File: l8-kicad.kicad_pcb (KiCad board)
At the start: 4 copper layers, 55.5 x 89.5 mm, 139 parts, among them J1 USB_B_Mini, J2 LCD 3.2" 240x320 Conn_01x14_P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, J3 Screw_Terminal_01x06, J4 Conn_ST_STDC14, J7 TC2030 - TAG Connect, Q1 SI2301CDS-T1-GE3, Q4 SI2301CDS-T1-GE3, Q5 SI2301CDS-T1-GE3, SW1 SW_Push, SW2 SW_Push, U1 B0505S-1WR2, U2 ISO1042-Q1, U22 TLV76733DRVx, U3 STM32F427V_G-I_Tx, U4 ST_SENSOR_2, U5 IIS3DHHCTR, X1 8MHz 20pF

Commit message: pre quilter - actually saved
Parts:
- added TP39: PD10, TestPoint:TestPoint_Pad_D1.0mm, F.Cu at (217.2, 168.3)
- added TP40: PD11, TestPoint:TestPoint_Pad_D1.0mm, F.Cu at (217.2, 171.3)
- TP27: value PD15 -> PD6
- TP28: value PD14 -> PD7
- TP29: value PD13 -> PD8
- TP30: value PD12 -> PD9
- moved TP10 169.7 mm to (217.2, 151.6)
- moved TP11 169.7 mm to (217.2, 154.6)
- moved TP12 169.7 mm to (217.2, 157.7)
- moved TP13 169.7 mm to (217.2, 160.7)
- moved TP14 169.7 mm to (217.2, 163.8)
- moved TP15 169.7 mm to (220.2, 145.4)
- moved TP16 169.7 mm to (220.2, 148.5)
- moved TP17 169.7 mm to (220.2, 151.6)
- moved TP18 169.7 mm to (220.2, 154.6)
- moved TP19 169.7 mm to (220.2, 157.7)
- moved TP20 169.7 mm to (220.2, 160.7)
- moved TP21 169.7 mm to (220.2, 163.8)
- moved TP22 169.7 mm to (223.2, 145.4)
- moved TP23 169.7 mm to (223.2, 148.5)
- moved TP24 169.7 mm to (223.2, 151.6)
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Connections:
- TP27 pad 1: /MCU/PD15 -> /MCU/PD6
- TP28 pad 1: /MCU/PD14 -> /MCU/PD7
- TP29 pad 1: /MCU/PD13 -> /MCU/PD8
- TP30 pad 1: /MCU/PD12 -> /MCU/PD9

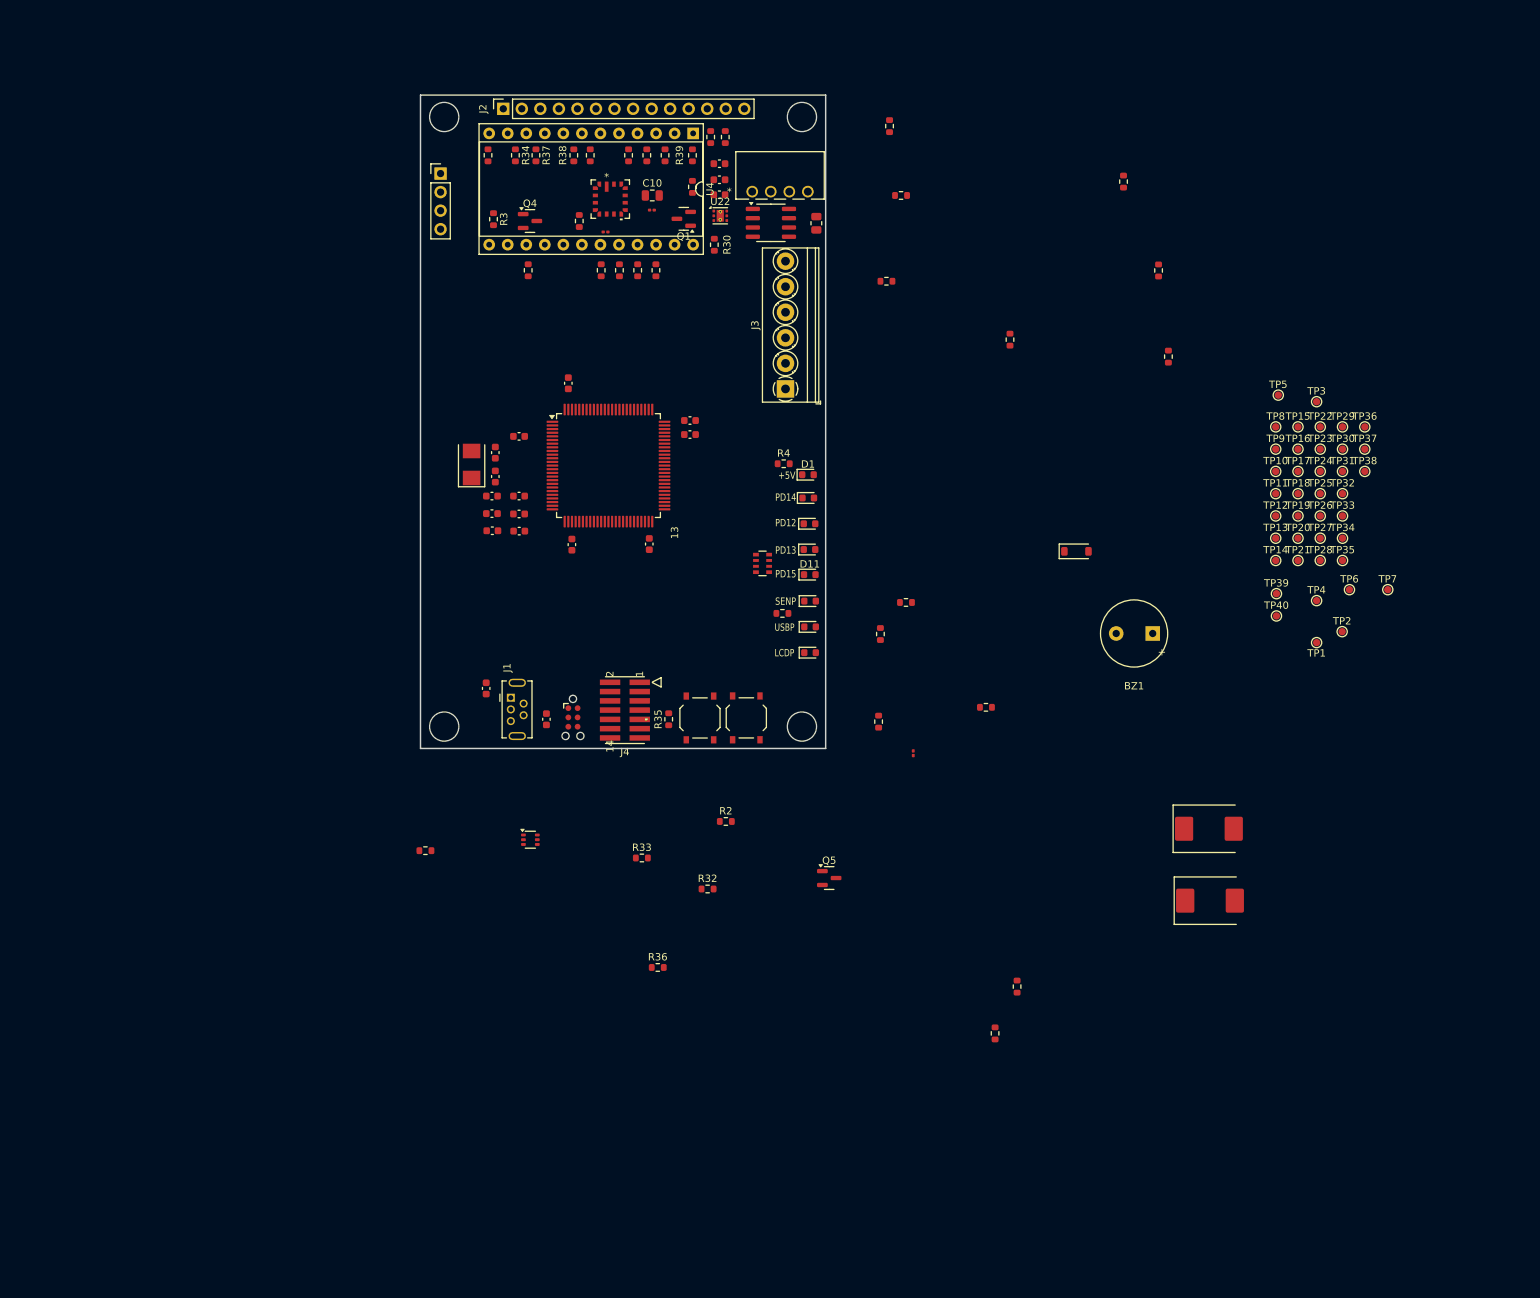
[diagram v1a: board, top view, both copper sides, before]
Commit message: remove tp and rotate cpu
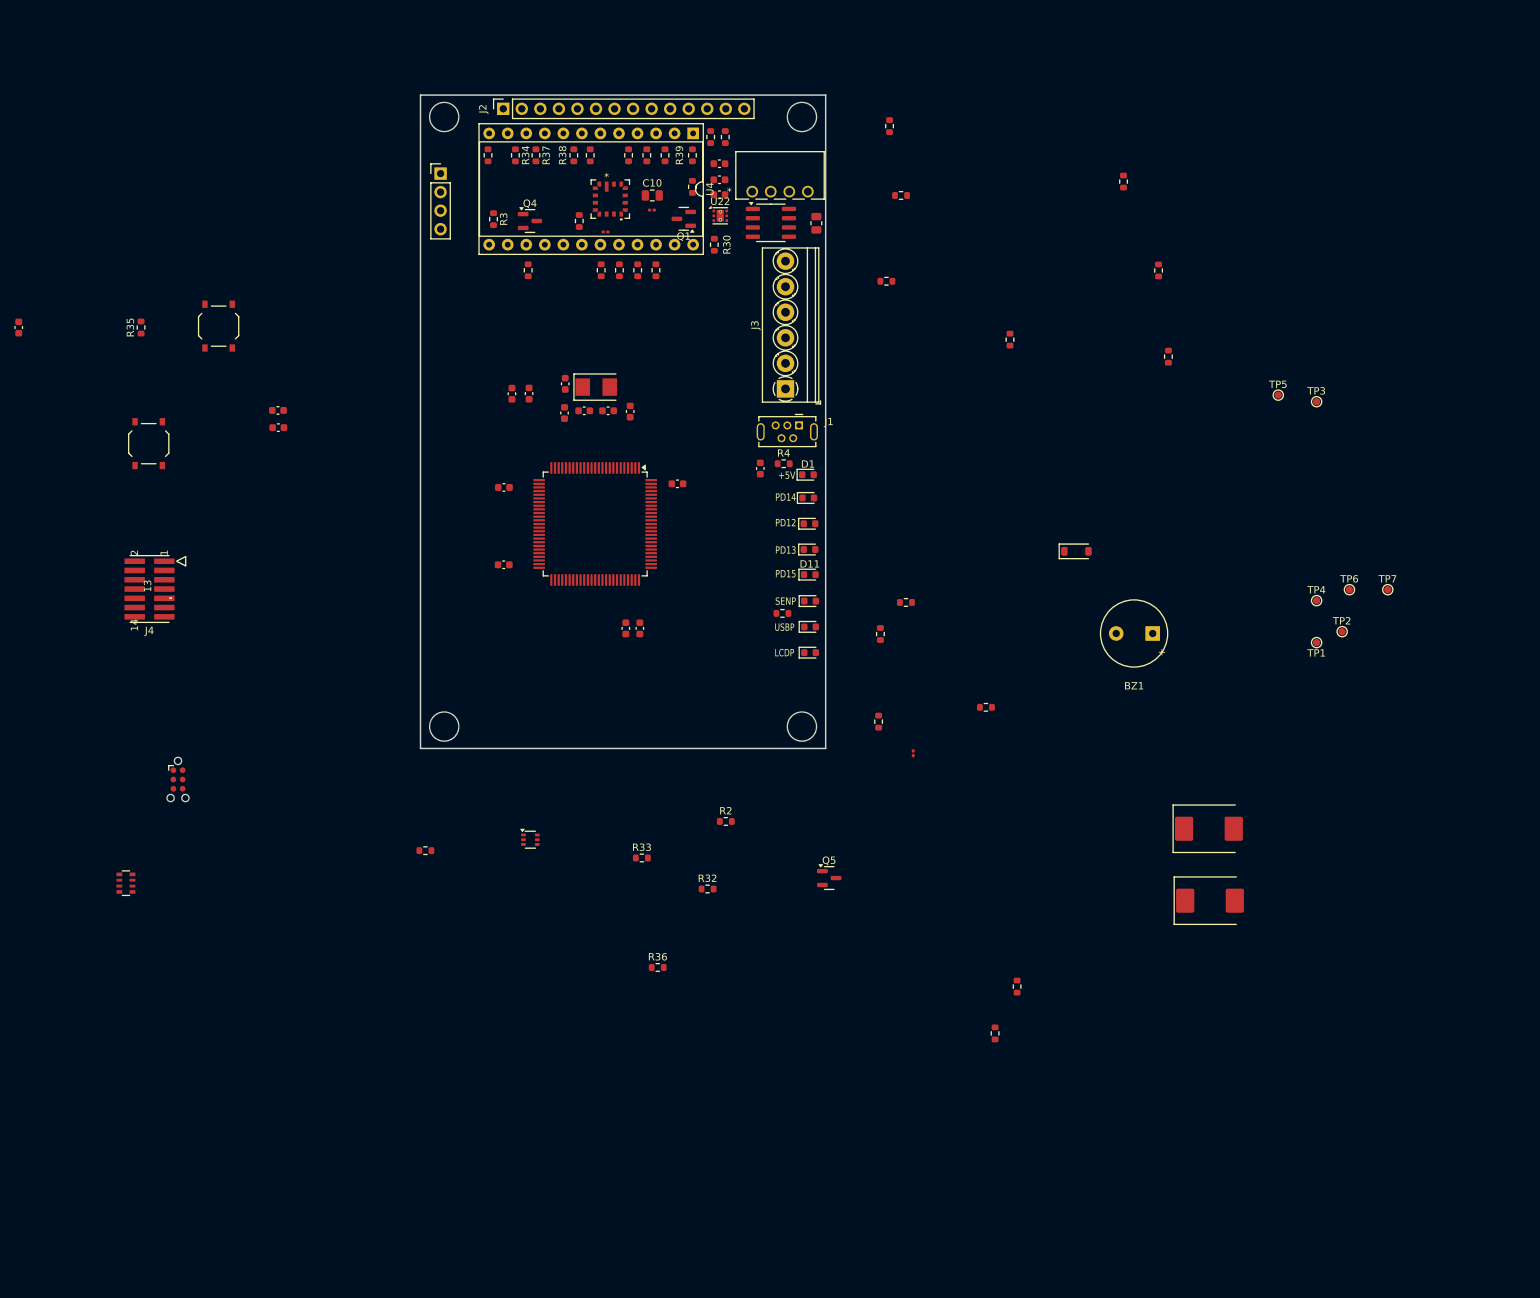
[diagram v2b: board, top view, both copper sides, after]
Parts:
- removed TP10: PC8, TestPoint:TestPoint_Pad_D1.0mm
- removed TP11: PC9, TestPoint:TestPoint_Pad_D1.0mm
- removed TP12: PC13, TestPoint:TestPoint_Pad_D1.0mm
- removed TP13: PC14, TestPoint:TestPoint_Pad_D1.0mm
- removed TP14: PC15, TestPoint:TestPoint_Pad_D1.0mm
- removed TP15: PC0, TestPoint:TestPoint_Pad_D1.0mm
- removed TP16: PA0, TestPoint:TestPoint_Pad_D1.0mm
- removed TP17: PA1, TestPoint:TestPoint_Pad_D1.0mm
- removed TP18: PA4, TestPoint:TestPoint_Pad_D1.0mm
- removed TP19: PA8, TestPoint:TestPoint_Pad_D1.0mm
- removed TP20: PB4, TestPoint:TestPoint_Pad_D1.0mm
- removed TP21: PB5, TestPoint:TestPoint_Pad_D1.0mm
- removed TP22: PB8, TestPoint:TestPoint_Pad_D1.0mm
- removed TP23: PB9, TestPoint:TestPoint_Pad_D1.0mm
- removed TP24: PB10, TestPoint:TestPoint_Pad_D1.0mm
- removed TP25: PB11, TestPoint:TestPoint_Pad_D1.0mm
- removed TP26: PB12, TestPoint:TestPoint_Pad_D1.0mm
- removed TP27: PD6, TestPoint:TestPoint_Pad_D1.0mm
- removed TP28: PD7, TestPoint:TestPoint_Pad_D1.0mm
- removed TP29: PD8, TestPoint:TestPoint_Pad_D1.0mm
- removed TP30: PD9, TestPoint:TestPoint_Pad_D1.0mm
- removed TP31: PE8, TestPoint:TestPoint_Pad_D1.0mm
- removed TP32: PE7, TestPoint:TestPoint_Pad_D1.0mm
- removed TP33: PE0, TestPoint:TestPoint_Pad_D1.0mm
- removed TP34: PE1, TestPoint:TestPoint_Pad_D1.0mm
- removed TP35: PE9, TestPoint:TestPoint_Pad_D1.0mm
- removed TP36: PE10, TestPoint:TestPoint_Pad_D1.0mm
- removed TP37: PE11, TestPoint:TestPoint_Pad_D1.0mm
- removed TP38: PE12, TestPoint:TestPoint_Pad_D1.0mm
- removed TP39: PD10, TestPoint:TestPoint_Pad_D1.0mm
- removed TP40: PD11, TestPoint:TestPoint_Pad_D1.0mm
- removed TP8: PC6, TestPoint:TestPoint_Pad_D1.0mm
- removed TP9: PC7, TestPoint:TestPoint_Pad_D1.0mm
- moved RN2 97.6 mm to (59.6, 207.9)
- moved C20 90.0 mm to (45.0, 131.8)
- moved R35 90.0 mm to (61.7, 131.8)
- moved SW2 90.0 mm to (72.3, 131.7)
- moved SW1 84.3 mm to (62.8, 147.8)
- moved J4 67.2 mm to (62.9, 167.7)
- moved J7 54.8 mm to (66.8, 193.8)
- moved J1 53.1 mm to (150.2, 146.1), turned to 180 degrees
- moved C37 48.1 mm to (146.6, 151.2), turned to 90 degrees
- moved C9 32.5 mm to (80.5, 143.2)
- moved C29 32.5 mm to (80.5, 145.6)
- moved C32 29.3 mm to (130.0, 173.1), turned to 90 degrees
- moved C1 28.0 mm to (128.1, 173.1), turned to -90 degrees
- moved C31 20.3 mm to (135.2, 153.2), turned to 0 degrees
- moved C8 20.1 mm to (111.4, 164.3), turned to 180 degrees
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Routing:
- added copper zone on In2.Cu, net +3.3V
- added copper zone on In1.Cu, net GND

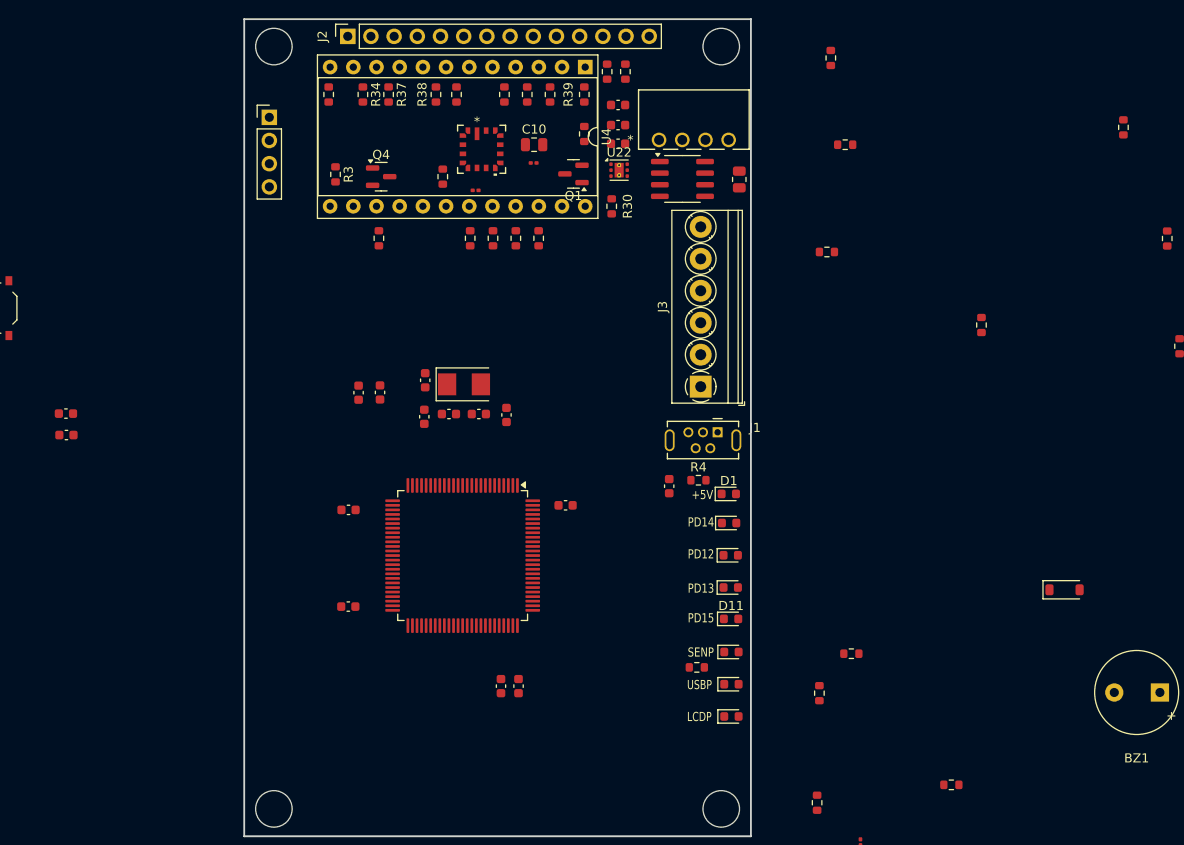
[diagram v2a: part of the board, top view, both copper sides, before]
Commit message: smaller caps remove ringing resistors
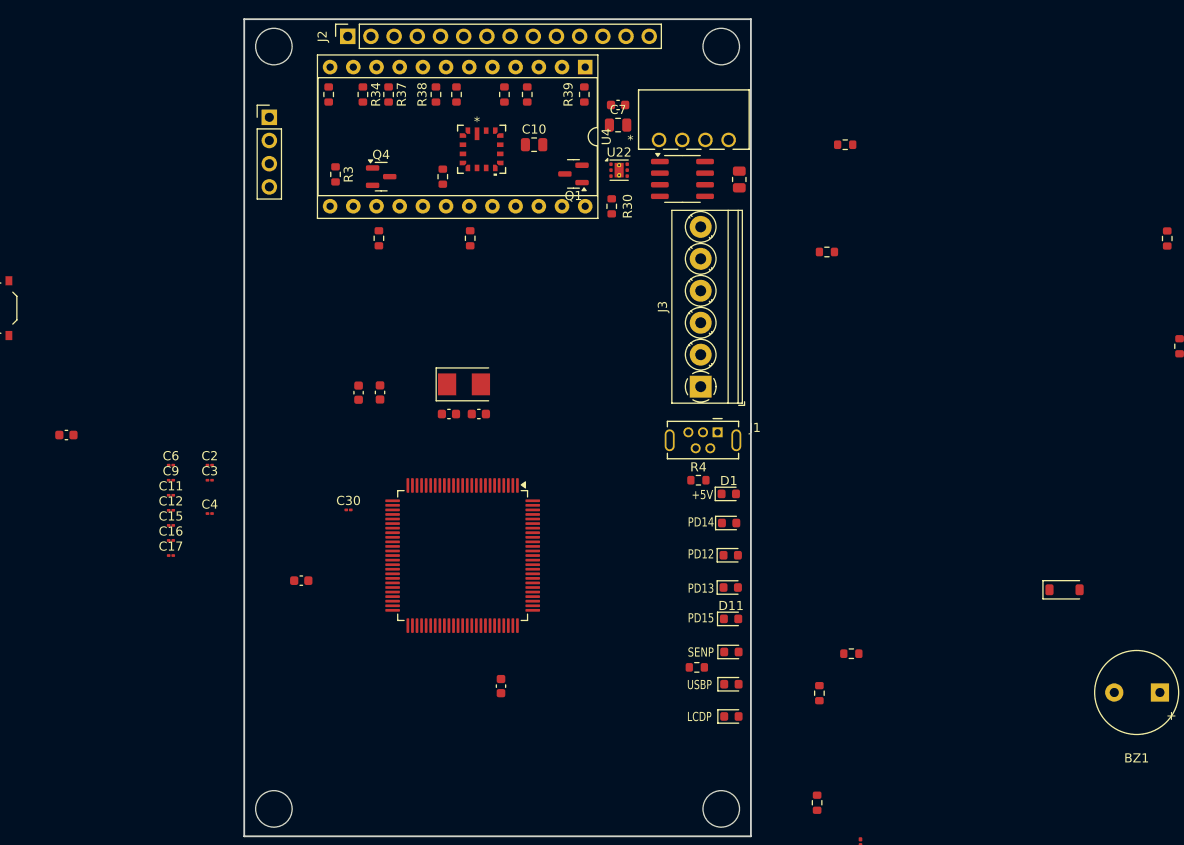
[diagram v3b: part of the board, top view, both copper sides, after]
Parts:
- removed C24, C31, C32, C33, C34, C37: 100nF, Capacitor_SMD:C_0603_1608Metric
- removed R17, R18, R19, R20, R21, R22, R23, R24, R25, R26, R31: 22R, Resistor_SMD:R_0603_1608Metric
- added C15: 100nF, Capacitor_SMD:C_01005_0402Metric, F.Cu at (92.0, 155.4)
- added C16: 100nF, Capacitor_SMD:C_01005_0402Metric, F.Cu at (92.0, 157.1)
- added C17: 100nF, Capacitor_SMD:C_01005_0402Metric, F.Cu at (92.0, 158.8)
- added C2: 100nF, Capacitor_SMD:C_01005_0402Metric, F.Cu at (96.2, 148.8)
- added C3: 100nF, Capacitor_SMD:C_01005_0402Metric, F.Cu at (96.2, 150.5)
- added C4: 100nF, Capacitor_SMD:C_01005_0402Metric, F.Cu at (96.2, 154.2)
- C11, C12: value 100nf -> 100nF; footprint Capacitor_SMD:C_0201_0603Metric -> Capacitor_SMD:C_01005_0402Metric
- C30, C6, C9: footprint Capacitor_SMD:C_0603_1608Metric -> Capacitor_SMD:C_01005_0402Metric
- C7: footprint Capacitor_SMD:C_0603_1608Metric -> Capacitor_SMD:C_0805_2012Metric
- R1: value 120 -> 120R
- R6: value 2.2k -> 2.2K
- moved C6 60.3 mm to (92.0, 148.8)
- moved C12 55.0 mm to (92.0, 153.8)
- moved C11 47.2 mm to (92.0, 152.2)
- moved C9 13.6 mm to (92.0, 150.5)
- moved C8 5.88 mm to (106.2, 161.5)
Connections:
- C11 pad 1: +3.3V -> GND
- C11 pad 2: Net-(Q1-D) -> +3.3V
- C12 pad 1: +3.3V -> GND
- C12 pad 2: Net-(Q1-D) -> +3.3V
- C6 pad 1: +3.3V -> /MCU/Shield
- C9 pad 1: GND -> Net-(U3-VDDA)
- C9 pad 2: +3.3V -> GND
- U3 pad 1: Net-(U3-PE2) -> /SPI4_SCK
- U3 pad 16: Net-(U3-PC1) -> /SPI2_CS
- U3 pad 17: Net-(U3-PC2) -> /SPI2_SDO
- U3 pad 18: Net-(U3-PC3) -> /SPI2_SDI
- U3 pad 2: Net-(U3-PE3) -> /SPI4_CS
- U3 pad 30: Net-(U3-PA5) -> /SPI1_SCK
- U3 pad 31: Net-(U3-PA6) -> /SPI1_SDI
- U3 pad 32: Net-(U3-PA7) -> /SPI1_SDO
- U3 pad 4: Net-(U3-PE5) -> /SPI4_SDI
- U3 pad 5: Net-(U3-PE6) -> /SPI4_SDO
- U3 pad 52: Net-(U3-PB13) -> /SPI2_SCK
